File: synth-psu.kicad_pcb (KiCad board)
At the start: 2 copper layers, 95 x 35 mm, 88 parts, among them J1 Conn_01x03_Male, J10 Conn_01x02_Male, J2 USB_C_Receptacle_16pin, J3 Conn_01x02_Male, J4 Conn_01x02_Male, J5 Conn_01x02_Male, J6 Conn_01x02_Male, J7 Conn_01x02_Male, J8 Conn_01x02_Male, J9 Conn_01x02_Male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

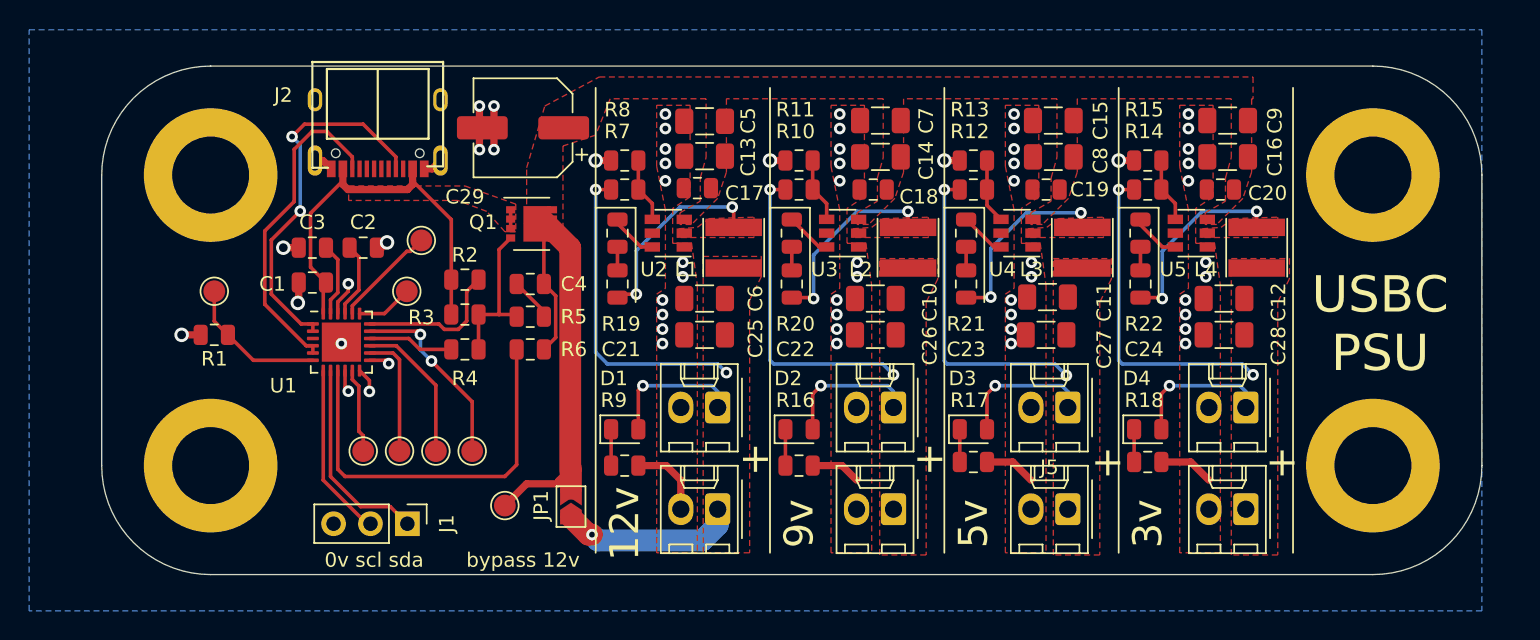
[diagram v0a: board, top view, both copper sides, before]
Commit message: shortened vfb traces
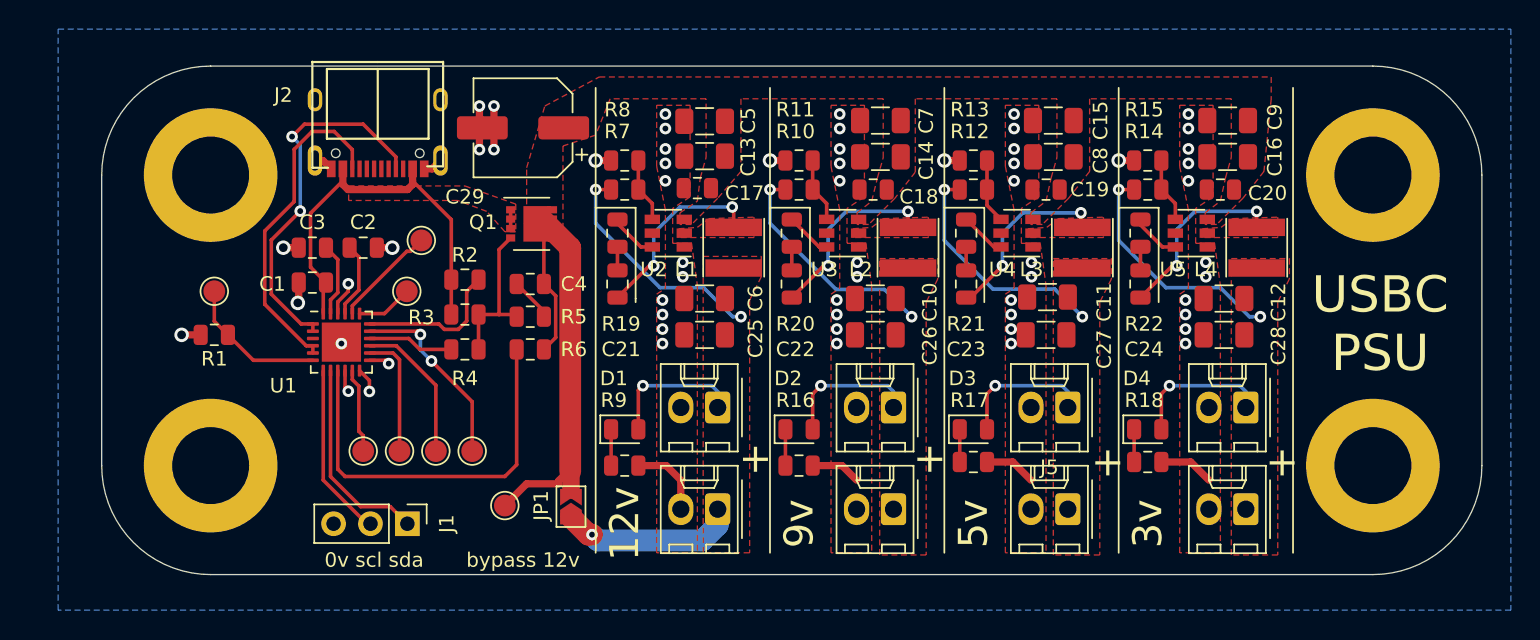
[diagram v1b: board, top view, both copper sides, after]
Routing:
- net +3V0: track 32.2 -> 26.2 mm
- net +9V: track 31.2 -> 25.3 mm
- net +12V: track 43.7 -> 37.9 mm
- net +5V: track 31.2 -> 25.7 mm
- net /sw_5: track 13.1 -> 12.4 mm

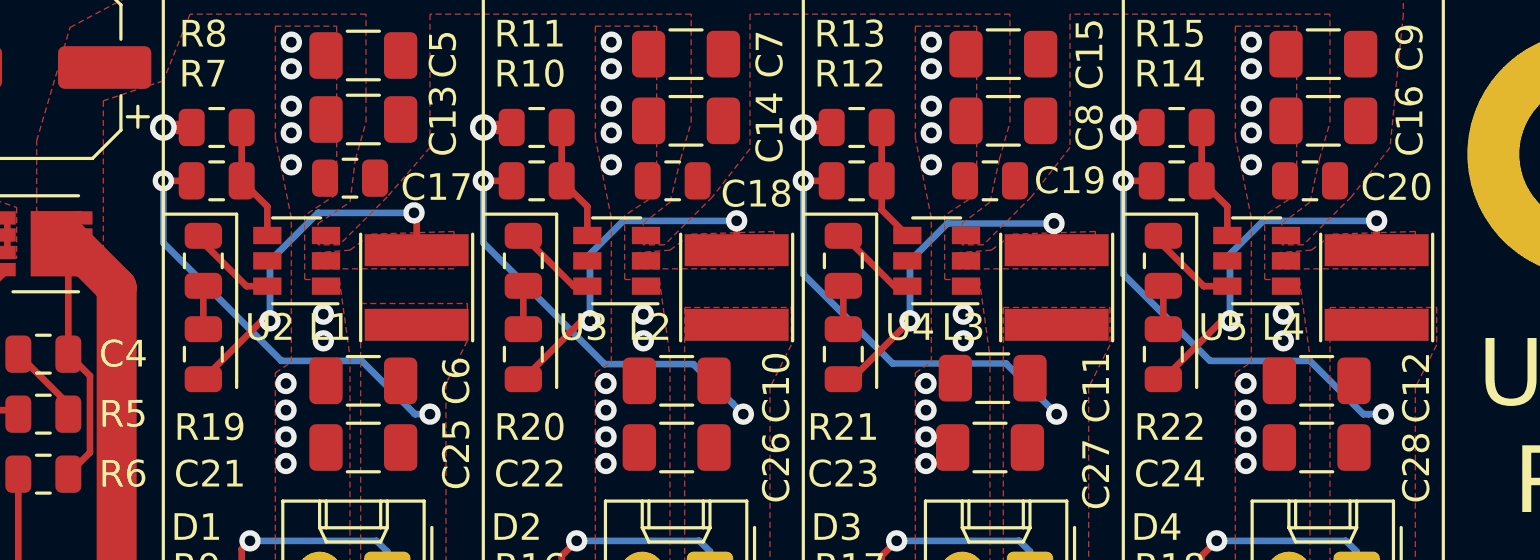
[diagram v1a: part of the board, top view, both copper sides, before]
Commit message: continue tweaking dc/dc copper pours
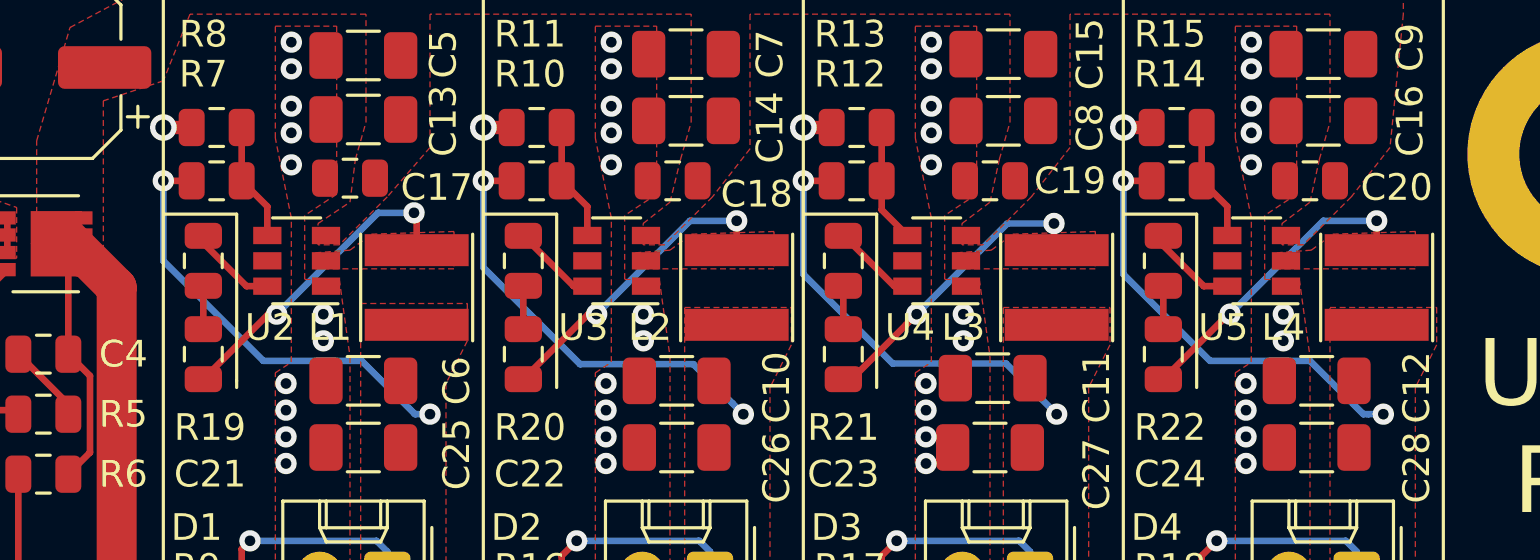
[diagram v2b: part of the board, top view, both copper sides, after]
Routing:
- net /sw_9: track 13.0 -> 11.6 mm
- net /sw_3: track 13.0 -> 11.6 mm
- net /sw_5: track 12.4 -> 11.1 mm
- net /sw_12v: track 13.2 -> 11.9 mm
- net +9V: track 25.3 -> 25.8 mm

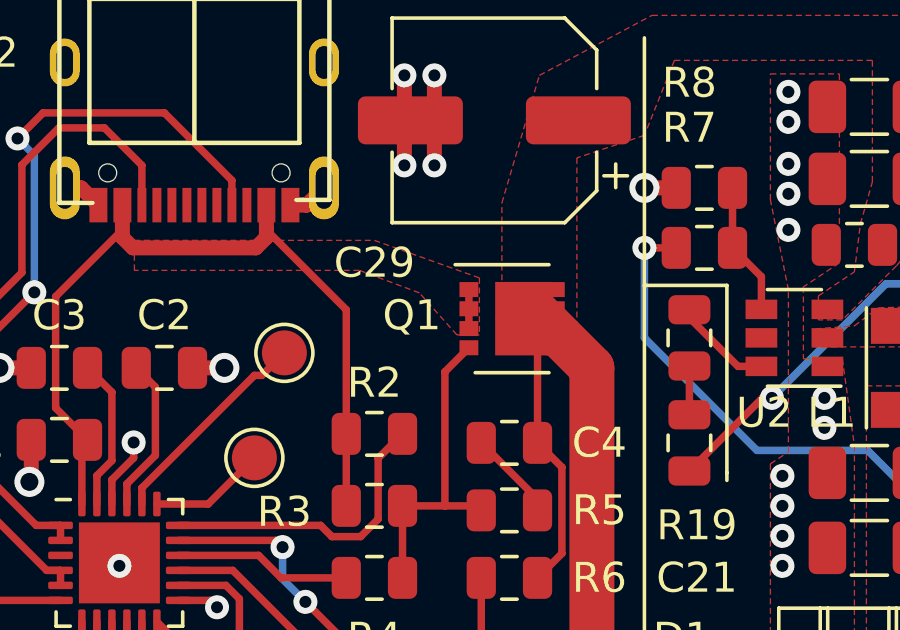
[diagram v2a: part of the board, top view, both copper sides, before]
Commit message: add vbus testpoint
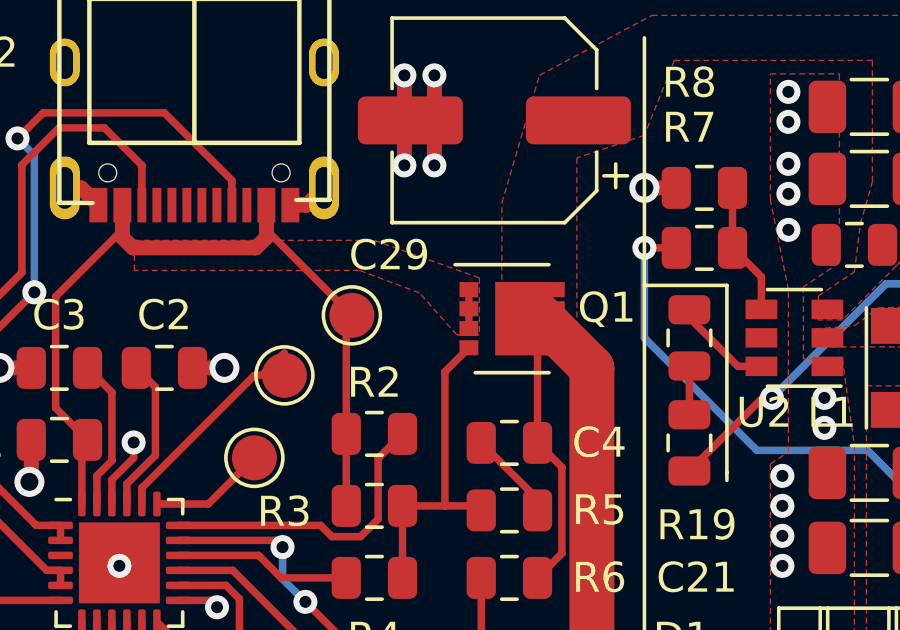
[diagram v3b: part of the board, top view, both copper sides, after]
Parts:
- added TP9: TestPoint, TestPoint:TestPoint_Pad_D1.5mm, F.Cu at (134.2, 73.2)
- R16: value 120k -> 466r
- R17: value 120k -> 200r
- R18: value 120k -> 90r
- R9: value 120k -> 660r
- U2, U3, U4, U5: value TPS562200 -> TPS56339
- moved TP2 0.75 mm to (132.0, 75.2)

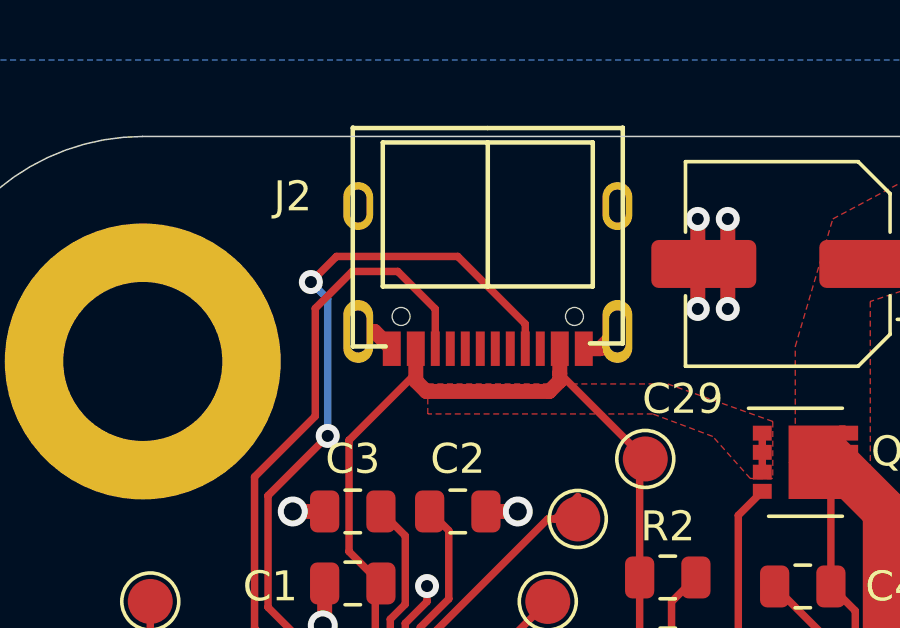
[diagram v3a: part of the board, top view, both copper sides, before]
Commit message: usb test pads
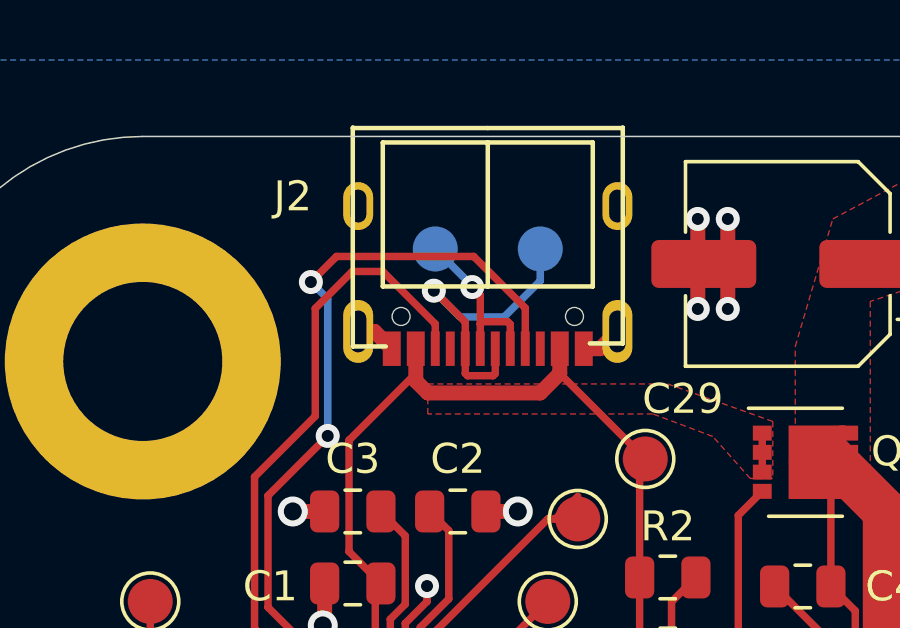
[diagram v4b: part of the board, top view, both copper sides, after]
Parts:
- added TP10: TestPoint, TestPoint:TestPoint_Pad_D1.5mm, B.Cu at (127.2, 66.2)
- added TP11: TestPoint, TestPoint:TestPoint_Pad_D1.5mm, B.Cu at (130.8, 66.2)
- C29: value 100uf 16v -> 100uf 25v
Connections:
- J2 pad A6: Net-(J2-PadA6) -> /d+
- J2 pad A7: Net-(J2-PadA7) -> /d-
- J2 pad B6: Net-(J2-PadB6) -> /d+
- J2 pad B7: Net-(J2-PadB7) -> /d-
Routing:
- net /d+: track 0.00 -> 10.5 mm, vias 0 -> 1
- net /d-: track 0.00 -> 5.82 mm, vias 0 -> 1
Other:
- board text added: "d+"
- board text added: "d-"

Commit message: push through bom changes to the pcb for the interactive bom viewer
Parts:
- C10, C11, C12, C25, C26, C27, C28, C6: value 22u -> 22u 16v
- C13, C14, C15, C16, C5, C7, C8, C9: value 10u -> 10u 25v
- C4: value 100nF -> 100n
- L1: value 20uH -> 6.8uH
- L2: value 24uH -> 6.8uH
- L3: value 5.6uH -> 6.8uH
- L4: value 13uH -> 6.8uH
- R10: value 102k -> 100k
- R12: value 52.3k -> 51k
- R16: value 466r -> 470r
- R18: value 90r -> 100r
- R5: value 100R -> 100r
